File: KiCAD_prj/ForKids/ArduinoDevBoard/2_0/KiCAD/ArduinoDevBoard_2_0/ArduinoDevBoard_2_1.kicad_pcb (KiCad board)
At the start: 2 copper layers, 44 parts, among them J1 Conn_01x04_Female, J10 Conn_01x04_Female, J11 Conn_01x04_Female, J12 Conn_01x02_Female, J13 Conn_01x15_Female, J14 Conn_01x15_Female, J2 Conn_01x04_Female, J3 Conn_01x05_Female, J4 Screw_Terminal_01x02, J5 Conn_01x02_Female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

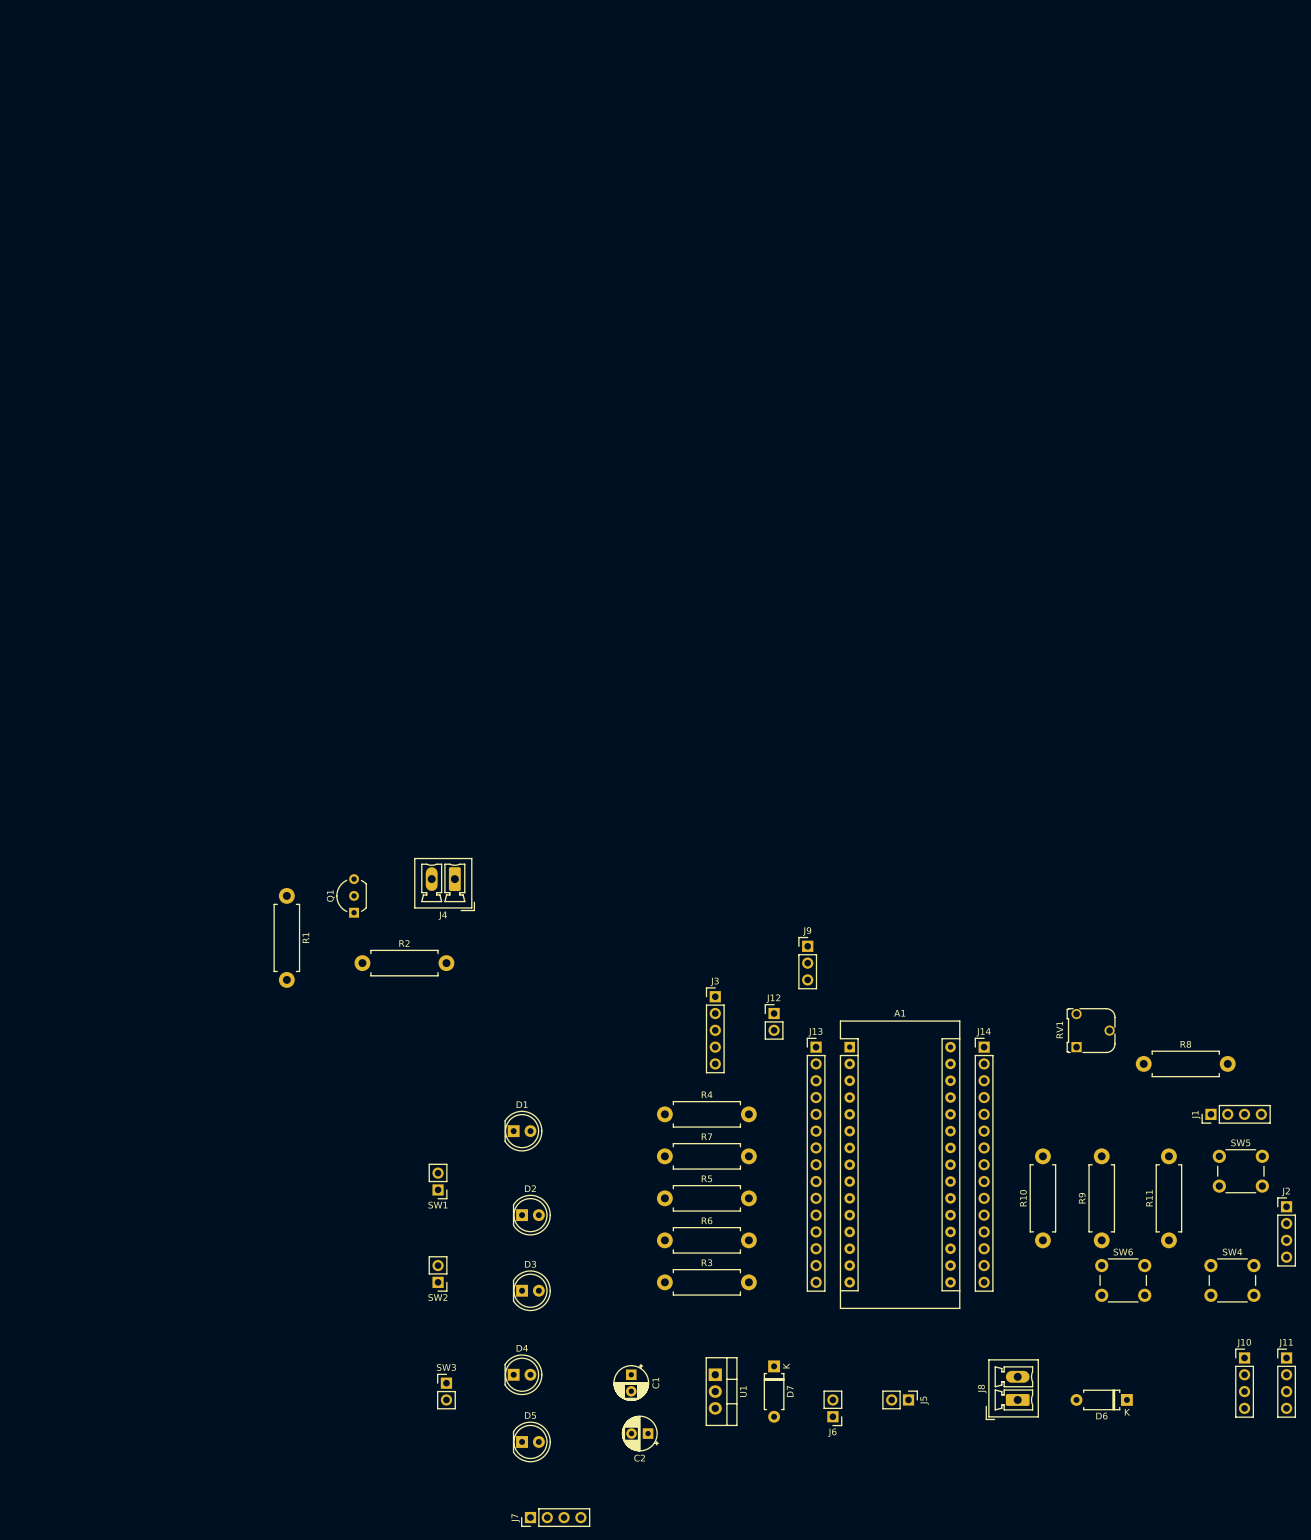
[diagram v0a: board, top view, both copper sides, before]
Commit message: Update  ArduinoDevBoard 2.1 project
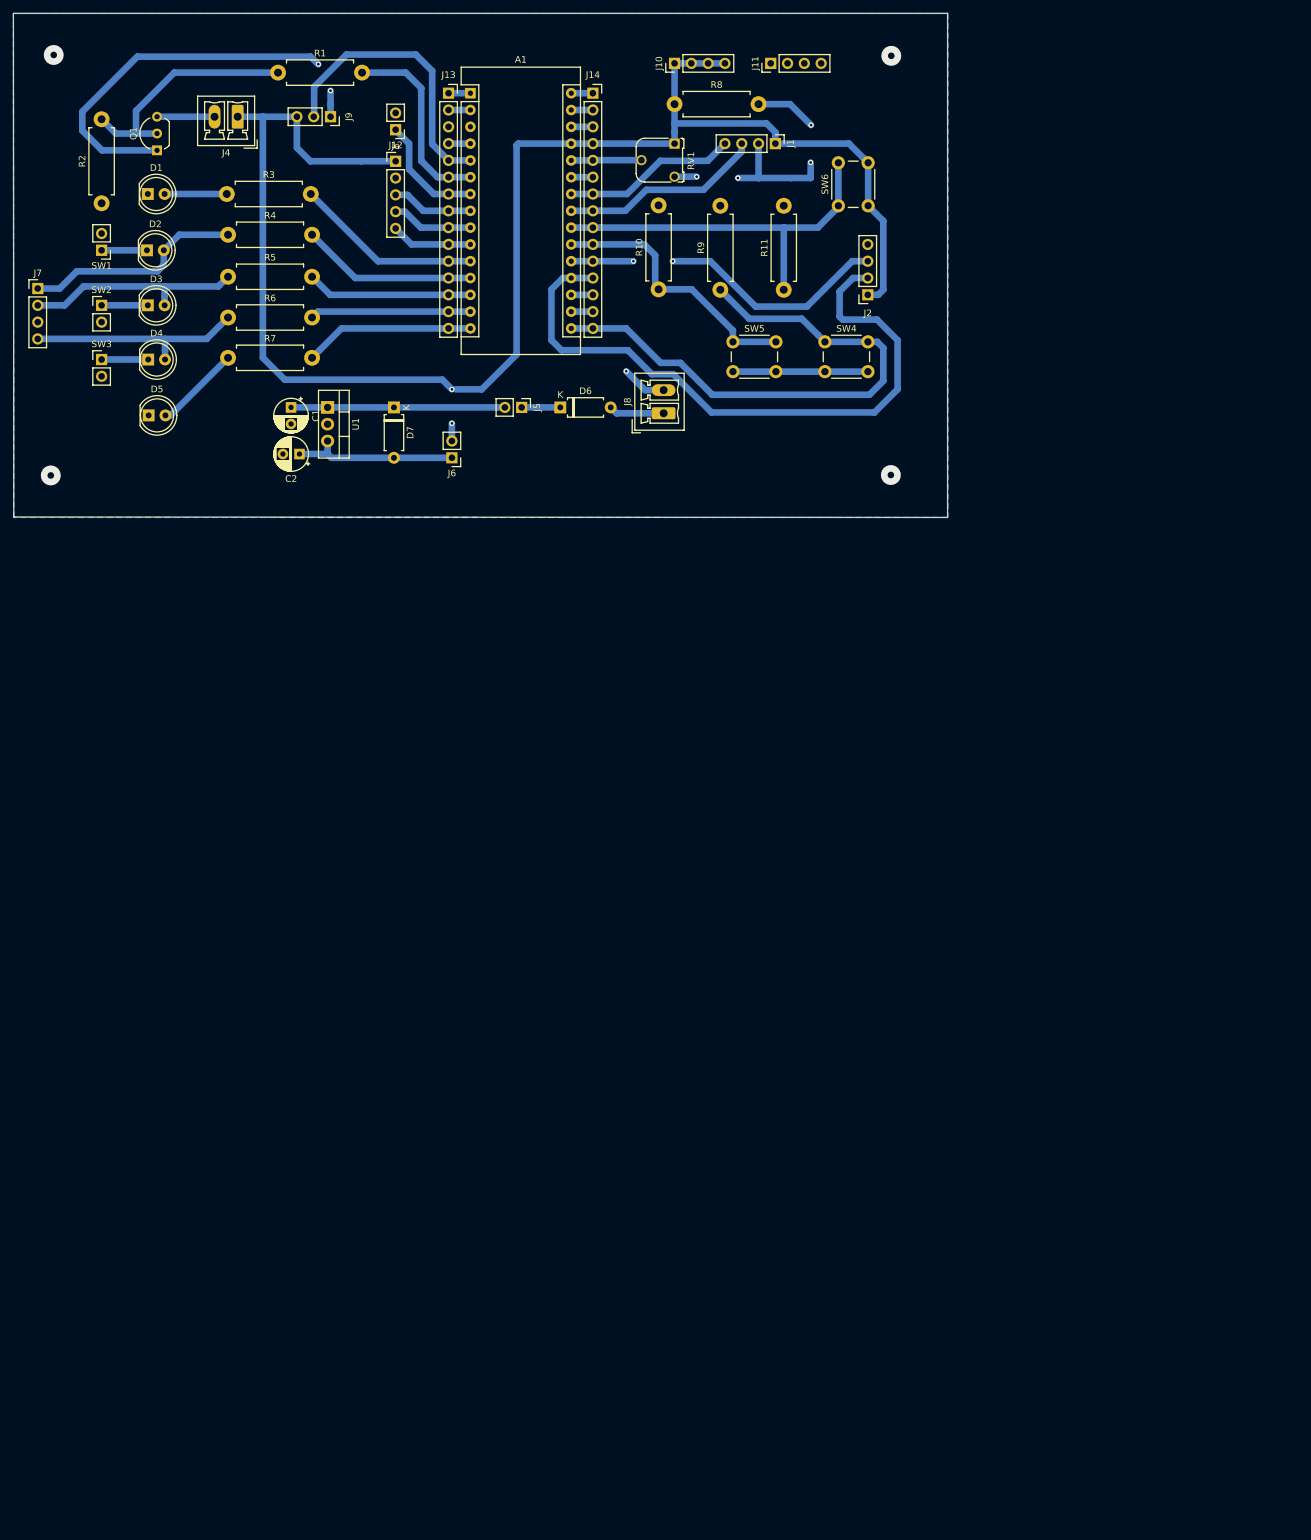
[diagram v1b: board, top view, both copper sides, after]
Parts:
- J13, J14: footprint Connector_PinHeader_2.54mm:PinHeader_1x15_P2.54mm_Vertical -> Connector_PinSocket_2.54mm:PinSocket_1x15_P2.54mm_Vertical
- J2: footprint Connector_PinHeader_2.54mm:PinHeader_1x04_P2.54mm_Vertical -> Connector_PinSocket_2.54mm:PinSocket_1x04_P2.54mm_Vertical
- J9: footprint Connector_PinHeader_2.54mm:PinHeader_1x03_P2.54mm_Vertical -> Connector_PinSocket_2.54mm:PinSocket_1x03_P2.54mm_Vertical
- moved J10 213.8 mm to (106.9, -68.7), turned to 90 degrees
- moved J11 210.7 mm to (121.4, -68.7), turned to 90 degrees
- moved J7 200.2 mm to (10.6, -34.7), turned to 0 degrees
- moved R3 177.4 mm to (39.2, -49.0)
- moved D6 172.8 mm to (89.6, -16.7), turned to 0 degrees
- moved D5 165.1 mm to (27.4, -15.5)
- moved SW6 165.1 mm to (131.6, -47.2), turned to 90 degrees
- moved SW3 163.3 mm to (20.3, -23.9)
- moved D4 163.1 mm to (27.3, -23.9)
- moved R8 161.5 mm to (106.9, -62.5)
- moved J5 161.0 mm to (83.8, -16.7)
- moved J1 160.8 mm to (122.1, -56.6), turned to 270 degrees
- moved D3 159.4 mm to (27.2, -32.1)
- moved J8 158.5 mm to (105.2, -15.8)
- moved U1 157.5 mm to (54.4, -16.7)
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- renumbered J3 to Je
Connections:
- A1 pad 3: RST -> Net-(A1-Pad3)
- J13 pad 1: RX -> TX
- J13 pad 2: TX -> RX
- J13 pad 3: RST -> Net-(J13-Pad3)
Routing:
- net +5V: track 0.00 -> 261.8 mm, vias 0 -> 2
- net Earth: track 0.00 -> 103.6 mm, vias 0 -> 7
- net A0: track 0.00 -> 99.5 mm
- net D13: track 0.00 -> 85.5 mm
- net A3: track 0.00 -> 57.8 mm
- net A1: track 0.00 -> 44.5 mm, vias 0 -> 2
- net D2: track 0.00 -> 43.3 mm
- net A2: track 0.00 -> 40.8 mm
- net Net-(Q1-Pad2): track 0.00 -> 36.6 mm
- net Net-(D2-Pad2): track 0.00 -> 33.4 mm
- net Net-(D3-Pad2): track 0.00 -> 33.4 mm
- net Net-(D4-Pad2): track 0.00 -> 33.2 mm
- net Net-(C1-Pad1): track 0.00 -> 32.3 mm
- net A4: track 0.00 -> 30.7 mm
- net D3: track 0.00 -> 29.4 mm
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- added copper zone on B.Cu, net Earth
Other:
- board outline added: 141.2 x 76.2 mm

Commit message: Update ArduinoDevBoard 2.1 rev  1.0
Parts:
- U1: footprint Package_TO_SOT_THT:TO-220-3_Vertical -> Package_TO_SOT_THT:TO-92_Wide
- moved U1 2.80 mm to (57.0, -15.7)
- moved J12 1.70 mm to (63.9, -60.1)
- moved C2 1.52 mm to (50.2, -8.13)
- moved C1 0.91 mm to (48.9, -15.8)
- moved D6 0.91 mm to (89.6, -15.8)
- moved D7 0.91 mm to (64.5, -15.8)
- moved J6 0.91 mm to (73.2, -8.17)
- moved J3 0.90 mm to (63.8, -53.9)
- moved J5 0.86 mm to (83.8, -15.8)
- moved J14 0.12 mm to (94.6, -64.2)
- renumbered Je to J3
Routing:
- net Earth: track 103.6 -> 56.8 mm, vias 7 -> 4
- net +5V: track 261.8 -> 272.9 mm, vias 2 -> 4
- net D13: track 85.5 -> 86.4 mm
- net D7: track 12.3 -> 13.2 mm
- net D6: track 12.3 -> 13.2 mm
- net D5: track 12.3 -> 13.2 mm
- net D3: track 29.4 -> 28.5 mm
- net A0: track 99.5 -> 100.4 mm
- net D4: track 17.6 -> 18.2 mm
